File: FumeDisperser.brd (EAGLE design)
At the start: 109.8 x 24.8 mm, 19 parts, among them IC1 MC34063AD

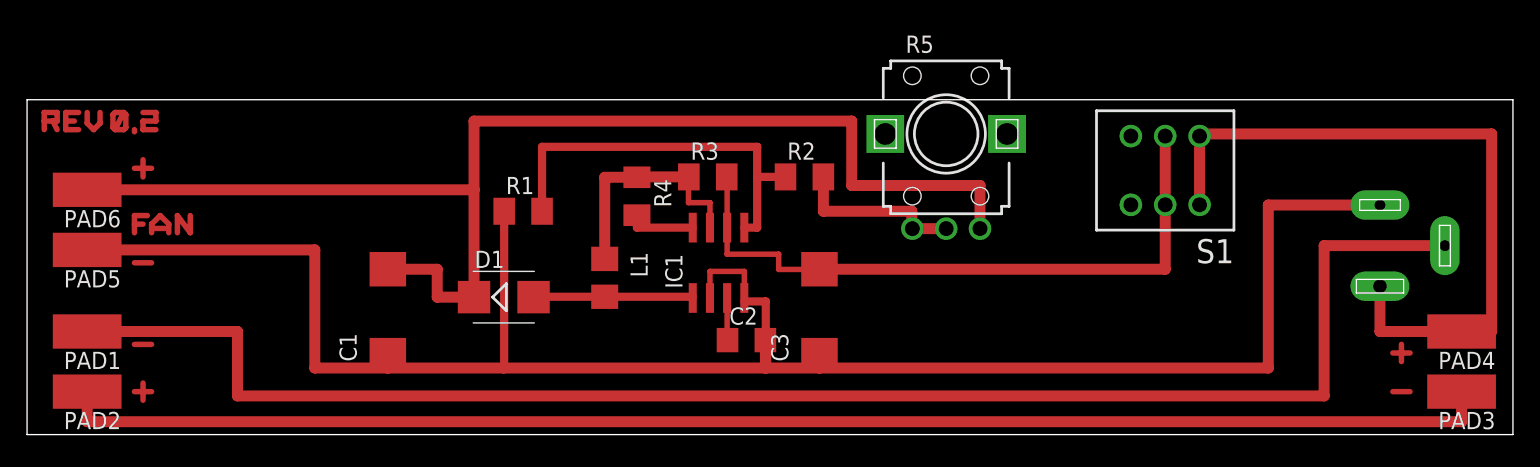
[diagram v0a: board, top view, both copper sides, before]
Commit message: Add PWM controller circuit
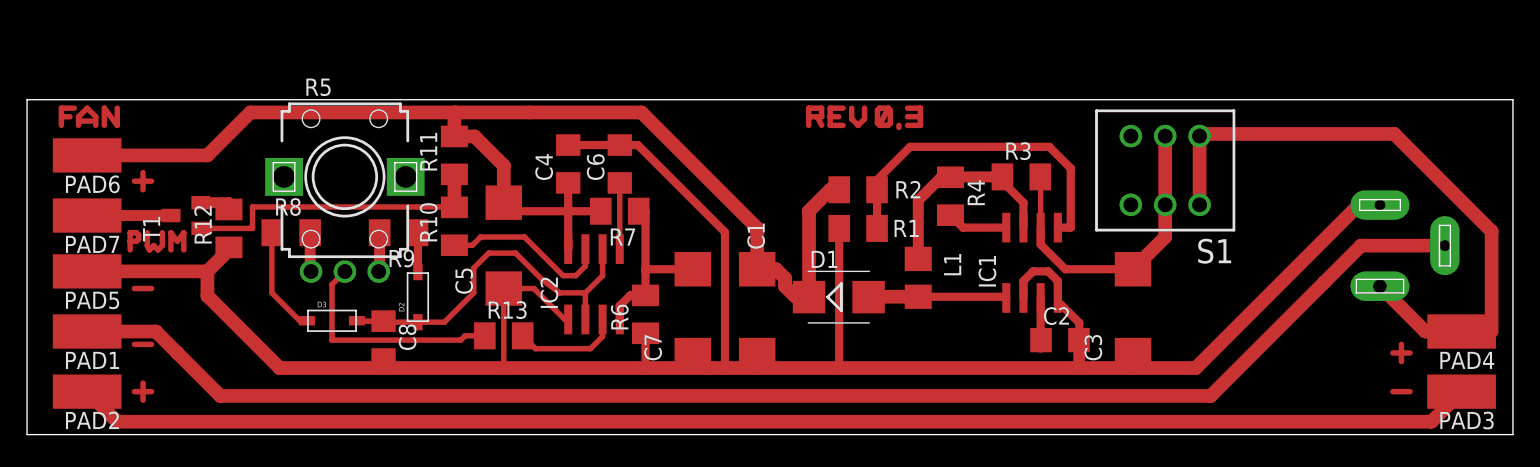
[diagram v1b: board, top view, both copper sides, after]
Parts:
- added C4, C6, C8: 0.1, resistor:C1206
- added C5: 10uF, rcl:D/7343-31R
- added C7: 220uF, rcl:D/7343-31R
- added D2, D3: (no value), adafruit:SOD-123
- added IC2: NE555D, linear:SO08
- added PAD7: Fan_PWM, wirepad:SMD2,54-5,08
- added R10, R8, R9: 1k, resistor:M1206
- added R11: 47k, resistor:M1206
- added R12, R13: 0, resistor:M1206
- added R6: 30k, resistor:M1206
- added R7: 150k, resistor:M1206
- added T1: bc817, transistor:SOT23-BEC
- R1: value 2.2k -> 3.9k
- R2: value 12k -> 33k
- moved R5 44.6 mm to (19.1, 19.1)
- moved C1 27.3 mm to (49.5, 9.05)
- moved R1 24.8 mm to (57.0, 15.2)
- moved D1 24.8 mm to (55.6, 10.2)
- moved R3 23.2 mm to (69.1, 19.1)
- moved C3 23.2 mm to (77.3, 9.05)
- moved L1 23.2 mm to (61.4, 11.6)
- moved R4 23.2 mm to (63.8, 17.6)
- moved C2 23.2 mm to (71.9, 6.99)
- moved IC1 23.2 mm to (69.8, 12.7)
- moved R2 4.08 mm to (57.0, 18.1), turned to 180 degrees
- moved PAD6 2.54 mm to (0.00, 20.6)
- moved PAD5 1.59 mm to (0.00, 12.1)
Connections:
- new net N$27: R13.1, R5.2
- new net N$29: C7.+, IC2.4, R6.2, R7.1
- new net N$30: D3.C, R8.1
- new net N$31: D2.A, R9.1
- new net N$32: R5.3, R9.2
- new net N$33: R5.1, R8.2
- new net N$34: IC2.3, R13.2
- new net N$35: IC2.7, R10.1
- new net N$36: R10.2, R11.1, T1.B
- new net N$37: PAD7.1, T1.C
- new net N$42: R12.2, T1.E
- new net VCC: C1.+, C4.1, C5.+, D1.C, IC2.8, PAD6.1, R11.2, R2.2, R7.2
- net GND: now also C4.2, C5.-, C6.2, C7.-, C8.2, IC2.1, R12.1, R6.1
- net N$11: now also C8.1, D2.C, D3.A, IC2.2, IC2.6; no longer R2.2, R5.1, R5.2
- net N$2: now also C6.1, IC2.5; no longer C1.+, D1.C, PAD6.1, R5.3
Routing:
- net VCC: track 0.00 -> 94.1 mm
- net N$2: track 95.6 -> 4.89 mm
- net GND: track 145.8 -> 174.2 mm
- net N$4: track 49.1 -> 23.4 mm
- net N$36: track 0.00 -> 22.8 mm
- net N$27: track 0.00 -> 16.9 mm
- net N$11: track 12.9 -> 27.0 mm
- net N$29: track 0.00 -> 13.4 mm
- net N$35: track 0.00 -> 12.7 mm
- net N$19: track 116.2 -> 106.9 mm
- net N$34: track 0.00 -> 7.93 mm
- net N$30: track 0.00 -> 7.92 mm
- net N$37: track 0.00 -> 6.20 mm
- net N$10: track 53.0 -> 46.9 mm
- net N$3: track 29.7 -> 24.9 mm
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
